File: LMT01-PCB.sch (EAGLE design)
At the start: 32 parts, among them IC1 PIC18F47Q84, IC2 +12v, IC3 LM393D, IC4 MAX3467CPA, IC5 LM393D

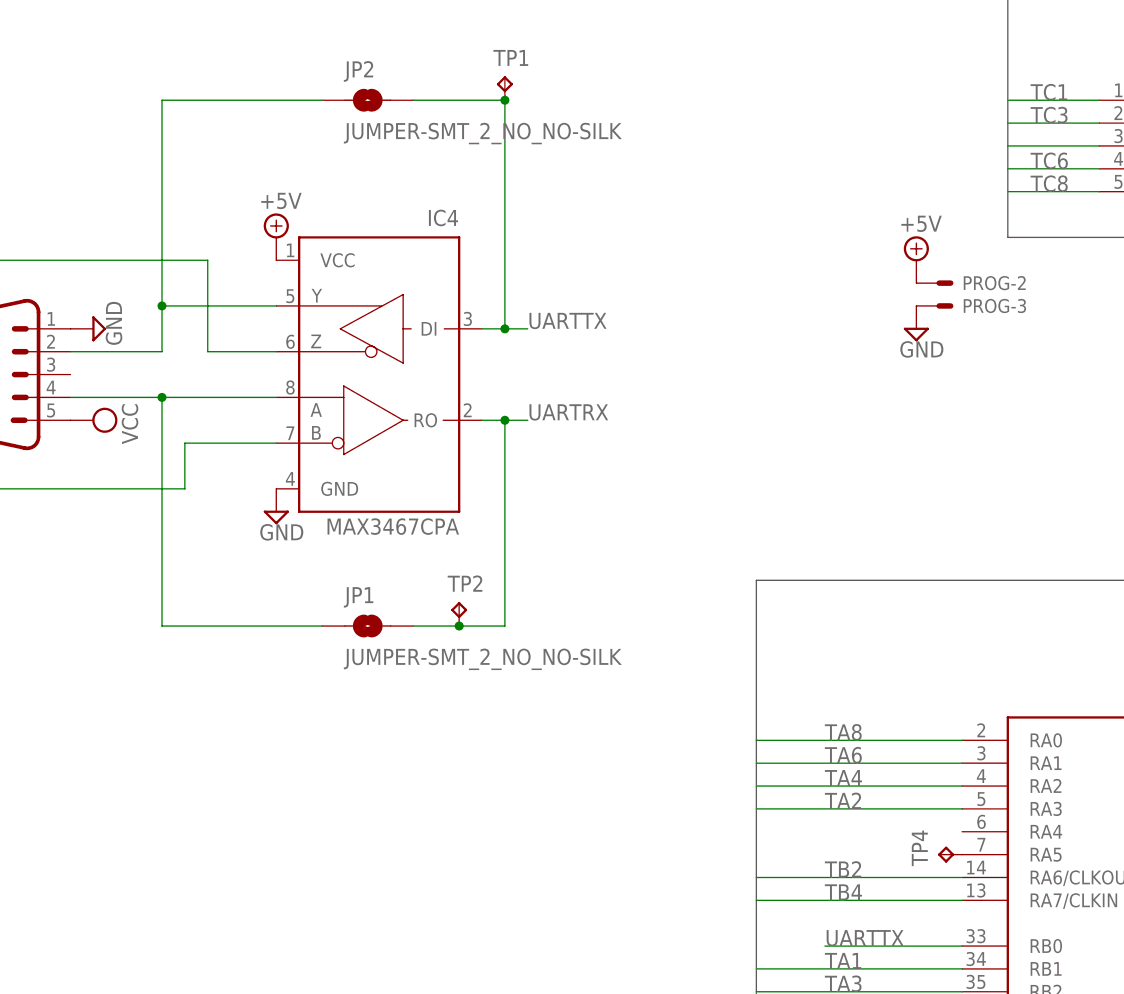
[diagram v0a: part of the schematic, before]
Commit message: Adding RS-485 capability
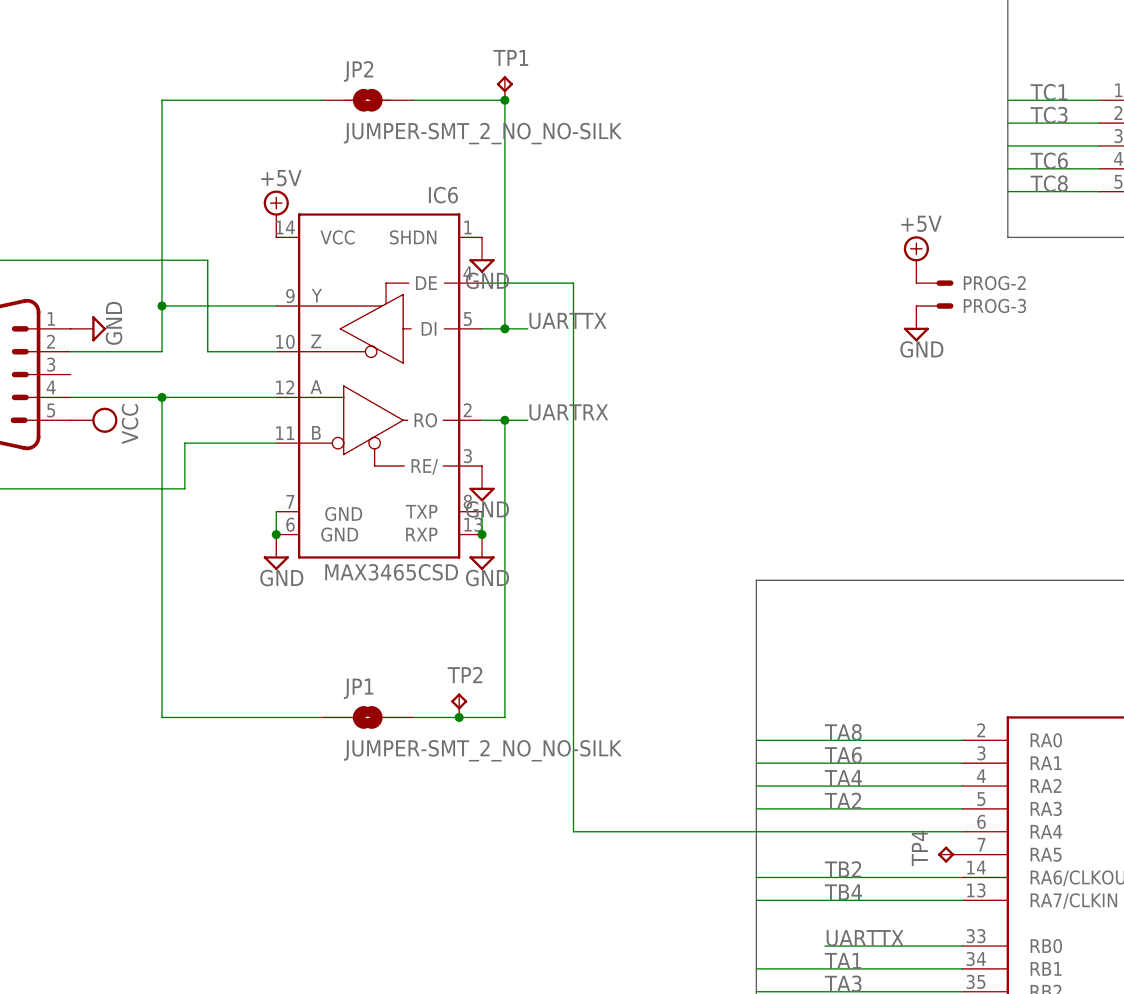
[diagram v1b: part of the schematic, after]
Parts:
- removed IC4: MAX3467CPA, maxim:MAX3467CPA
- added IC6: MAX3465CSD, maxim:MAX3465CSD
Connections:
- new net N$9: IC1.RA4, IC6.DE
- net +5V: now also IC6.VCC; no longer IC4.VCC
- net GND: now also IC6.GND, IC6.GND@1, IC6.RE/, IC6.RXP, IC6.SHDN, IC6.TXP; no longer IC4.GND
- net RX+: now also IC6.A; no longer IC4.A
- net RX-: now also IC6.B; no longer IC4.B
- net TX+: now also IC6.Y; no longer IC4.Y
- net TX-: now also IC6.Z; no longer IC4.Z
- net UARTRX: now also IC6.RO; no longer IC4.RO
- net UARTTX: now also IC6.DI; no longer IC4.DI
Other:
- moved on the sheet: JP1, TP2
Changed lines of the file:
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@@
 <part name="SUPPLY8" library="supply2" deviceset="+5V" device=""/>
 <part name="X2" library="con-subd" deviceset="M09" device="HP"/>
-<part name="IC4" library="maxim" deviceset="MAX3467*" device="PA" technology="C"/>
 <part name="SUPPLY9" library="supply2" deviceset="GND" device=""/>
 <part name="SUPPLY10" library="supply2" deviceset="+5V" device=""/>
@@
 <part name="TP7" library="testpad" deviceset="TP" device="B1,27"/>
 <part name="TP8" library="testpad" deviceset="TP" device="B1,27"/>
+<part name="IC6" library="maxim" deviceset="MAX346*" device="SD" technology="5C"/>
+<part name="SUPPLY34" library="supply2" deviceset="GND" device=""/>
+<part name="SUPPLY35" library="supply2" deviceset="GND" device=""/>
+<part name="SUPPLY36" library="supply2" deviceset="GND" device=""/>
 </parts>
 <sheets>
@@
 <instance part="SUPPLY8" gate="+5V" x="40.64" y="-81.28"/>
 <instance part="X2" gate="-1" x="-101.6" y="-50.8"/>
-<instance part="IC4" gate="G$1" x="-58.42" y="-50.8" rot="MR0"/>
-<instance part="SUPPLY9" gate="GND" x="-71.12" y="-66.04"/>
-<instance part="SUPPLY10" gate="+5V" x="-71.12" y="-35.56"/>
+<instance part="SUPPLY9" gate="GND" x="-71.12" y="-71.12"/>
+<instance part="SUPPLY10" gate="+5V" x="-71.12" y="-33.02"/>
 <instance part="SUPPLY11" gate="GND" x="-91.44" y="-45.72" rot="R90"/>
 <instance part="SUPPLY12" gate="GND" x="-111.76" y="-45.72" rot="R270"/>
@@
 <instance part="SUPPLY14" gate="G$1" x="-91.44" y="-55.88" rot="R270"/>
 <instance part="SUPPLY15" gate="G$1" x="-96.52" y="93.98"/>
-<instance part="JP1" gate="G$1" x="-60.96" y="-78.74"/>
+<instance part="JP1" gate="G$1" x="-60.96" y="-88.9"/>
 <instance part="JP2" gate="G$1" x="-60.96" y="-20.32"/>
 <instance part="R1" gate="G$1" x="55.88" y="-60.96" rot="R90"/>
@@
 <instance part="SUPPLY18" gate="GND" x="0" y="-45.72"/>
 <instance part="TP1" gate="G$1" x="-45.72" y="-17.78"/>
-<instance part="TP2" gate="G$1" x="-50.8" y="-76.2"/>
+<instance part="TP2" gate="G$1" x="-50.8" y="-86.36"/>
 <instance part="SUPPLY1" gate="GND" x="45.72" y="-157.48"/>
 <instance part="SUPPLY2" gate="+5V" x="45.72" y="-81.28"/>
@@
 <instance part="TP7" gate="G$1" x="99.06" y="-45.72"/>
 <instance part="TP8" gate="G$1" x="139.7" y="-45.72"/>
+<instance part="IC6" gate="G$1" x="-58.42" y="-53.34" rot="MR0"/>
+<instance part="SUPPLY34" gate="GND" x="-48.26" y="-38.1"/>
+<instance part="SUPPLY35" gate="GND" x="-48.26" y="-63.5"/>
+<instance part="SUPPLY36" gate="GND" x="-48.26" y="-71.12"/>
 </instances>
 <busses>
@@
 <net name="+5V" class="0">
 <segment>
-<pinref part="IC4" gate="G$1" pin="VCC"/>
-<pinref part="SUPPLY10" gate="+5V" pin="+5V"/>
-</segment>
-<segment>
 <pinref part="PROG" gate="-2" pin="S"/>
 <pinref part="SUPPLY17" gate="+5V" pin="+5V"/>
@@
 <pinref part="SUPPLY33" gate="+5V" pin="+5V"/>
 </segment>
+<segment>
+<pinref part="IC6" gate="G$1" pin="VCC"/>
+<pinref part="SUPPLY10" gate="+5V" pin="+5V"/>
+</segment>
 </net>
 <net name="GND" class="0">
-<segment>
-<pinref part="IC4" gate="G$1" pin="GND"/>
-<pinref part="SUPPLY9" gate="GND" pin="GND"/>
-</segment>
 <segment>
 <pinref part="X2" gate="-1" pin="1"/>
@@
 <pinref part="SUPPLY32" gate="GND" pin="GND"/>
 </segment>
+<segment>
+<pinref part="IC6" gate="G$1" pin="GND"/>
+<pinref part="SUPPLY9" gate="GND" pin="GND"/>
+<pinref part="IC6" gate="G$1" pin="GND@1"/>
+<wire x1="-71.12" y1="-66.04" x2="-71.12" y2="-68.58" width="0.1524" layer="91"/>
+<junction x="-71.12" y="-68.58"/>
+</segment>
+<segment>
+<pinref part="IC6" gate="G$1" pin="SHDN"/>
+<pinref part="SUPPLY34" gate="GND" pin="GND"/>
+</segment>
+<segment>
+<pinref part="IC6" gate="G$1" pin="RE/"/>
+<pinref part="SUPPLY35" gate="GND" pin="GND"/>
+</segment>
+<segment>
+<pinref part="IC6" gate="G$1" pin="TXP"/>
+<pinref part="IC6" gate="G$1" pin="RXP"/>
+<wire x1="-48.26" y1="-66.04" x2="-48.26" y2="-68.58" width="0.1524" layer="91"/>
+<pinref part="SUPPLY36" gate="GND" pin="GND"/>
+<junction x="-48.26" y="-68.58"/>
+</segment>
 </net>
 <net name="UARTRX" class="0">
 <segment>
-<pinref part="IC4" gate="G$1" pin="RO"/>
 <wire x1="-48.26" y1="-55.88" x2="-45.72" y2="-55.88" width="0.1524" layer="91"/>
 <label x="-43.18" y="-55.88" size="1.778" layer="95"/>
 <wire x1="-45.72" y1="-55.88" x2="-43.18" y2="-55.88" width="0.1524" layer="91"/>
-<wire x1="-45.72" y1="-55.88" x2="-45.72" y2="-78.74" width="0.1524" layer="91"/>
+<wire x1="-45.72" y1="-55.88" x2="-45.72" y2="-88.9" width="0.1524" layer="91"/>
 <junction x="-45.72" y="-55.88"/>
 <pinref part="JP1" gate="G$1" pin="2"/>
-<wire x1="-45.72" y1="-78.74" x2="-50.8" y2="-78.74" width="0.1524" layer="91"/>
+<wire x1="-45.72" y1="-88.9" x2="-50.8" y2="-88.9" width="0.1524" layer="91"/>
 <pinref part="TP2" gate="G$1" pin="TP"/>
-<wire x1="-50.8" y1="-78.74" x2="-55.88" y2="-78.74" width="0.1524" layer="91"/>
-<junction x="-50.8" y="-78.74"/>
+<wire x1="-50.8" y1="-88.9" x2="-55.88" y2="-88.9" width="0.1524" layer="91"/>
+<junction x="-50.8" y="-88.9"/>
+<pinref part="IC6" gate="G$1" pin="RO"/>
 </segment>
 <segment>
@@
 <net name="UARTTX" class="0">
 <segment>
-<pinref part="IC4" gate="G$1" pin="DI"/>
 <wire x1="-48.26" y1="-45.72" x2="-45.72" y2="-45.72" width="0.1524" layer="91"/>
 <label x="-43.18" y="-45.72" size="1.778" layer="95"/>
@@
 <pinref part="TP1" gate="G$1" pin="TP"/>
 <junction x="-45.72" y="-20.32"/>
+<pinref part="IC6" gate="G$1" pin="DI"/>
 </segment>
 <segment>
@@
 <net name="TX+" class="0">
 <segment>
-<pinref part="IC4" gate="G$1" pin="Y"/>
 <wire x1="-71.12" y1="-43.18" x2="-83.82" y2="-43.18" width="0.1524" layer="91"/>
 <wire x1="-83.82" y1="-43.18" x2="-83.82" y2="-48.26" width="0.1524" layer="91"/>
@@
 <wire x1="-83.82" y1="-43.18" x2="-83.82" y2="-20.32" width="0.1524" layer="91"/>
 <junction x="-83.82" y="-43.18"/>
+<pinref part="IC6" gate="G$1" pin="Y"/>
 </segment>
 </net>
 <net name="TX-" class="0">
 <segment>
-<pinref part="IC4" gate="G$1" pin="Z"/>
 <wire x1="-71.12" y1="-48.26" x2="-78.74" y2="-48.26" width="0.1524" layer="91"/>
 <wire x1="-78.74" y1="-48.26" x2="-78.74" y2="-38.1" width="0.1524" layer="91"/>
@@
 <pinref part="X2" gate="-1" pin="7"/>
 <wire x1="-116.84" y1="-48.26" x2="-109.22" y2="-48.26" width="0.1524" layer="91"/>
+<pinref part="IC6" gate="G$1" pin="Z"/>
 </segment>
 </net>
 <net name="RX+" class="0">
 <segment>
-<pinref part="IC4" gate="G$1" pin="A"/>
 <pinref part="X2" gate="-1" pin="4"/>
 <wire x1="-71.12" y1="-53.34" x2="-83.82" y2="-53.34" width="0.1524" layer="91"/>
 <wire x1="-83.82" y1="-53.34" x2="-93.98" y2="-53.34" width="0.1524" layer="91"/>
-<wire x1="-83.82" y1="-53.34" x2="-83.82" y2="-78.74" width="0.1524" layer="91"/>
+<wire x1="-83.82" y1="-53.34" x2="-83.82" y2="-88.9" width="0.1524" layer="91"/>
 <junction x="-83.82" y="-53.34"/>
 <pinref part="JP1" gate="G$1" pin="1"/>
-<wire x1="-66.04" y1="-78.74" x2="-83.82" y2="-78.74" width="0.1524" layer="91"/>
+<wire x1="-66.04" y1="-88.9" x2="-83.82" y2="-88.9" width="0.1524" layer="91"/>
+<pinref part="IC6" gate="G$1" pin="A"/>
 </segment>
 </net>
 <net name="RX-" class="0">
 <segment>
-<pinref part="IC4" gate="G$1" pin="B"/>
 <wire x1="-71.12" y1="-58.42" x2="-81.28" y2="-58.42" width="0.1524" layer="91"/>
 <wire x1="-81.28" y1="-58.42" x2="-81.28" y2="-63.5" width="0.1524" layer="91"/>
@@
 <pinref part="X2" gate="-1" pin="8"/>
 <wire x1="-116.84" y1="-50.8" x2="-109.22" y2="-50.8" width="0.1524" layer="91"/>
+<pinref part="IC6" gate="G$1" pin="B"/>
 </segment>
 </net>
@@
 </segment>
 </net>
+<net name="N$9" class="0">
+<segment>
+<pinref part="IC1" gate="G$1" pin="RA4"/>
+<wire x1="5.08" y1="-101.6" x2="-38.1" y2="-101.6" width="0.1524" layer="91"/>
+<wire x1="-38.1" y1="-101.6" x2="-38.1" y2="-40.64" width="0.1524" layer="91"/>
+<pinref part="IC6" gate="G$1" pin="DE"/>
+<wire x1="-38.1" y1="-40.64" x2="-48.26" y2="-40.64" width="0.1524" layer="91"/>
+</segment>
+</net>

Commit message: Adding pullup resistor on MCLR
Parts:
- added R6: 5k, resistor:R-US_R1206
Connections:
- net +5V: now also R6.2
- net N$1: now also R6.1
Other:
- moved on the sheet: PROG-1
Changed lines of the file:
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@@
 <part name="SUPPLY35" library="supply2" deviceset="GND" device=""/>
 <part name="SUPPLY36" library="supply2" deviceset="GND" device=""/>
+<part name="R6" library="resistor" deviceset="R-US_" device="R1206" value="5k"/>
+<part name="SUPPLY37" library="supply2" deviceset="+5V" device=""/>
 </parts>
 <sheets>
@@
 <instance part="R1" gate="G$1" x="55.88" y="-60.96" rot="R90"/>
 <instance part="SUPPLY16" gate="GND" x="55.88" y="-68.58"/>
-<instance part="PROG" gate="-1" x="83.82" y="-144.78"/>
+<instance part="PROG" gate="-1" x="124.46" y="-144.78"/>
 <instance part="PROG" gate="-2" x="2.54" y="-40.64"/>
 <instance part="PROG" gate="-3" x="2.54" y="-43.18"/>
@@
 <instance part="SUPPLY35" gate="GND" x="-48.26" y="-63.5"/>
 <instance part="SUPPLY36" gate="GND" x="-48.26" y="-71.12"/>
+<instance part="R6" gate="G$1" x="119.38" y="-139.7" rot="R90"/>
+<instance part="SUPPLY37" gate="+5V" x="119.38" y="-132.08"/>
 </instances>
 <busses>
@@
 <pinref part="IC6" gate="G$1" pin="VCC"/>
 <pinref part="SUPPLY10" gate="+5V" pin="+5V"/>
+</segment>
+<segment>
+<pinref part="R6" gate="G$1" pin="2"/>
+<pinref part="SUPPLY37" gate="+5V" pin="+5V"/>
 </segment>
 </net>
@@
 <pinref part="IC1" gate="G$1" pin="RE3/!MCLR"/>
 <pinref part="PROG" gate="-1" pin="S"/>
-<wire x1="81.28" y1="-144.78" x2="78.74" y2="-144.78" width="0.1524" layer="91"/>
-</segment>
-</net>
+<wire x1="121.92" y1="-144.78" x2="119.38" y2="-144.78" width="0.1524" layer="91"/>
+<pinref part="R6" gate="G$1" pin="1"/>
+<wire x1="119.38" y1="-144.78" x2="78.74" y2="-144.78" width="0.1524" layer="91"/>
+<junction x="119.38" y="-144.78"/>
+</segment>
+</net>
